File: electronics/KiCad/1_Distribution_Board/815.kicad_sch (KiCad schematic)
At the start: 45 parts, among them J12 Conn_01x06, J13 Conn_01x10, J14 2.54-1*4P母, J15 2.54-1*4P母, J16 PM254V-11-06-H85, J17 Conn_02x08_Odd_Even, J18 PM254V-11-06-H85, J19 2.54-1*4P母, J20 2.54-1*4P母, U6 PCA9306, U7 PCA9685PW, Y1 25MHz

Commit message: Correcting Part rotation for JLCPCB
Several parts needed the "FT Rotation Offset" parameter added to correct for part orientation for JLCPCB order.
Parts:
- U6: LCSC C33196 -> C123752
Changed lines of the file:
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@@
 			)
 		)
-		(property "LCSC" "C33196"
+		(property "LCSC" "C123752"
 			(at 52.07 46.99 0)
 			(effects

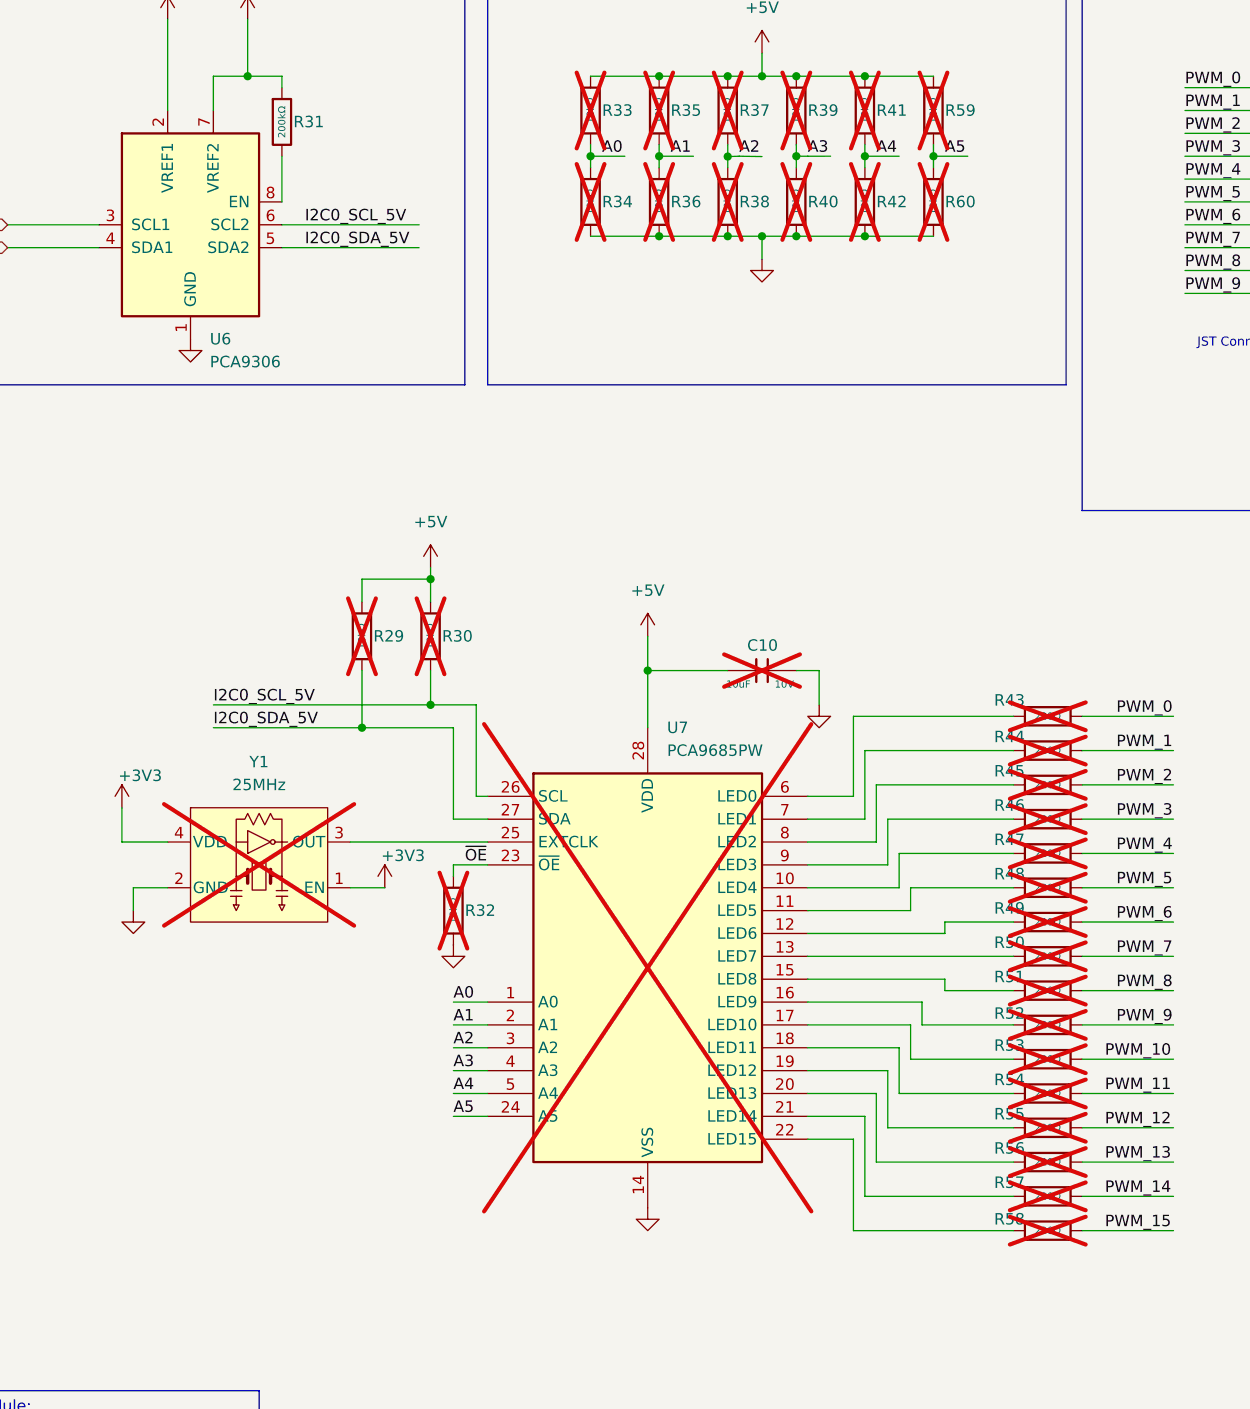
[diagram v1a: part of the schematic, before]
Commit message: Updated to reflect V1.0 of layer board as well
Updated for initial orders with PCA module populated. Also updated to layer boards for flex cables.
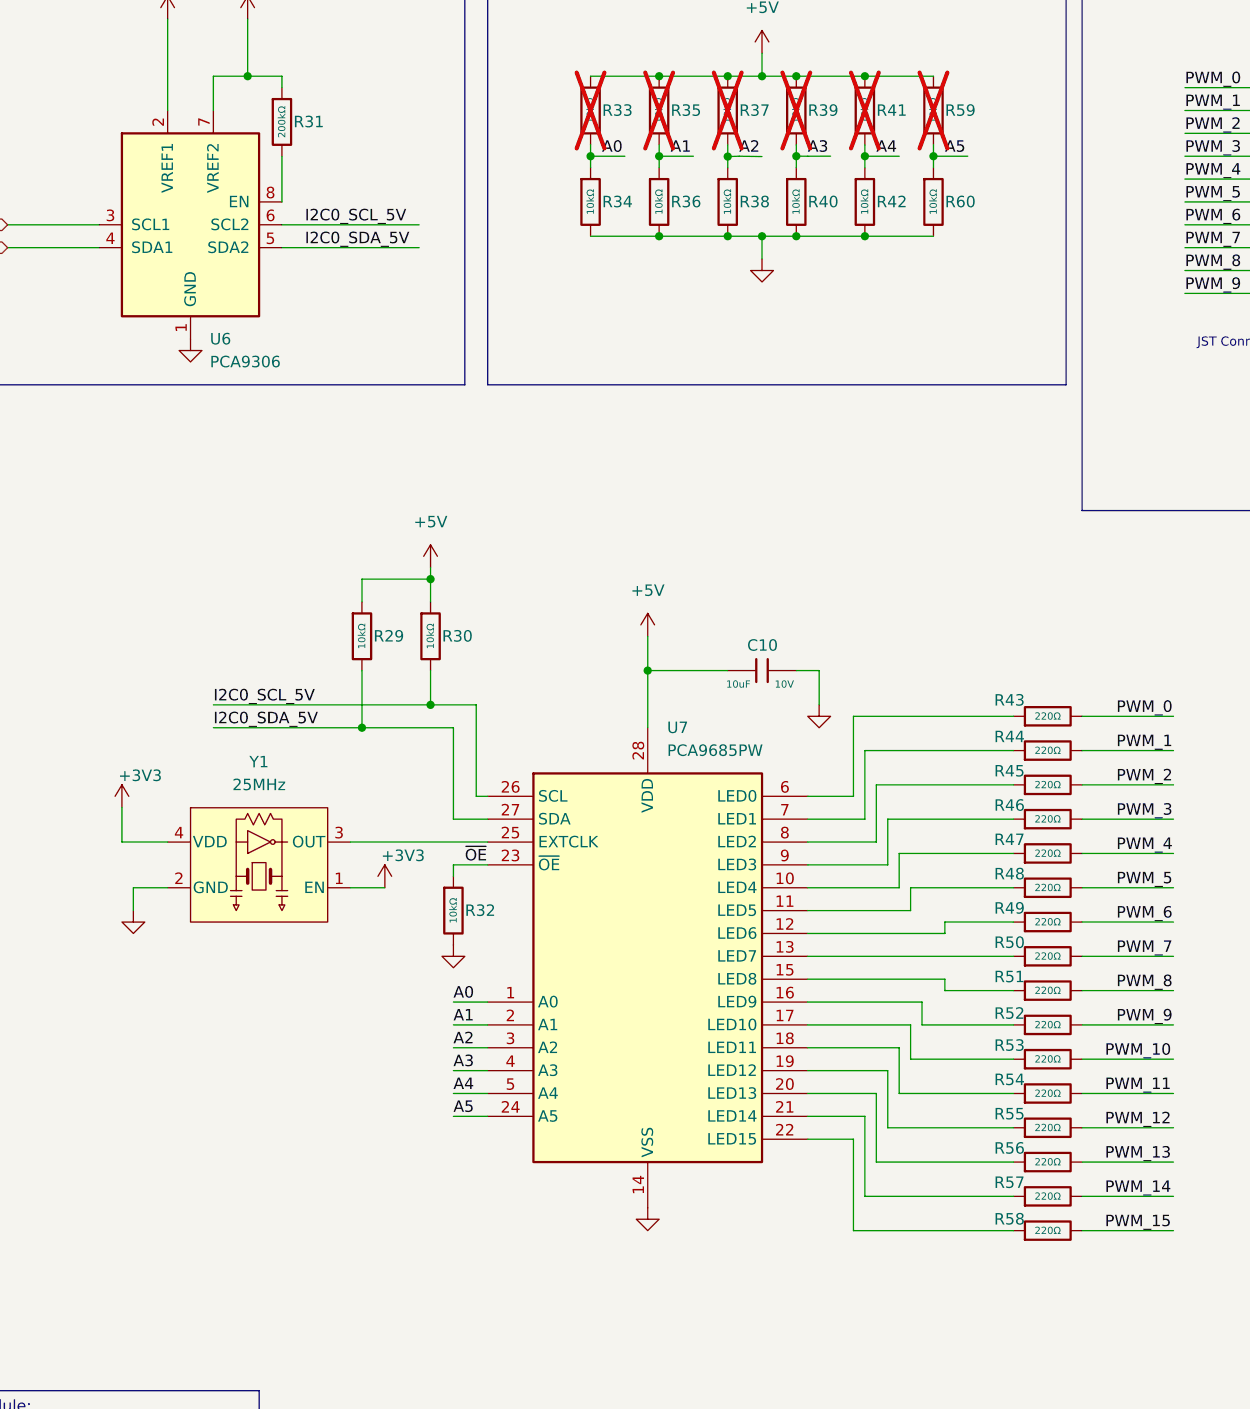
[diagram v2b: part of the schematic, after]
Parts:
- C10, R29, R30, R32, R34, R36, R38, R40, R42, R43, R44, R45, R46, R47, R48, R49, R50, R51, R52, R53, R54, R55, R56, R57, R58, R60, U7, Y1: now fitted
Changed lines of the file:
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@@
 		(in_bom yes)
 		(on_board yes)
-		(dnp yes)
+		(dnp no)
 		(property "Reference" "R53"
 			(at 144.78 138.176 90)
@@
 		(in_bom yes)
 		(on_board yes)
-		(dnp yes)
+		(dnp no)
 		(fields_autoplaced yes)
 		(property "Reference" "U7"
@@
 		(in_bom yes)
 		(on_board yes)
-		(dnp yes)
+		(dnp no)
 		(property "Reference" "R55"
 			(at 144.78 145.796 90)
@@
 		(in_bom yes)
 		(on_board yes)
-		(dnp yes)
+		(dnp no)
 		(property "Reference" "R38"
 			(at 113.03 44.45 0)
@@
 		(in_bom yes)
 		(on_board yes)
-		(dnp yes)
+		(dnp no)
 		(property "Reference" "R50"
 			(at 144.78 126.746 90)
@@
 		(in_bom yes)
 		(on_board yes)
-		(dnp yes)
+		(dnp no)
 		(property "Reference" "R54"
 			(at 144.78 141.986 90)
@@
 		(in_bom yes)
 		(on_board yes)
-		(dnp yes)
+		(dnp no)
 		(property "Reference" "R40"
 			(at 120.65 44.45 0)
@@
 		(in_bom yes)
 		(on_board yes)
-		(dnp yes)
+		(dnp no)
 		(property "Reference" "R52"
 			(at 144.78 134.62 90)
@@
 		(in_bom yes)
 		(on_board yes)
-		(dnp yes)
+		(dnp no)
 		(property "Reference" "R60"
 			(at 135.89 44.45 0)
@@
 		(in_bom yes)
 		(on_board yes)
-		(dnp yes)
+		(dnp no)
 		(property "Reference" "R36"
 			(at 105.41 44.45 0)
@@
 		(in_bom yes)
 		(on_board yes)
-		(dnp yes)
+		(dnp no)
 		(property "Reference" "R34"
 			(at 97.79 44.45 0)
@@
 		(in_bom yes)
 		(on_board yes)
-		(dnp yes)
+		(dnp no)
 		(property "Reference" "R46"
 			(at 144.78 111.506 90)
@@
 		(in_bom yes)
 		(on_board yes)
-		(dnp yes)
+		(dnp no)
 		(property "Reference" "R49"
 			(at 144.78 122.936 90)
@@
 		(in_bom yes)
 		(on_board yes)
-		(dnp yes)
+		(dnp no)
 		(property "Reference" "R42"
 			(at 128.27 44.45 0)
@@
 		(in_bom yes)
 		(on_board yes)
-		(dnp yes)
+		(dnp no)
 		(property "Reference" "R29"
 			(at 72.39 92.71 0)
@@
 		(in_bom yes)
 		(on_board yes)
-		(dnp yes)
+		(dnp no)
 		(fields_autoplaced yes)
 		(property "Reference" "Y1"
@@
 		(in_bom yes)
 		(on_board yes)
-		(dnp yes)
+		(dnp no)
 		(property "Reference" "R44"
 			(at 144.78 103.886 90)
@@
 		(in_bom yes)
 		(on_board yes)
-		(dnp yes)
+		(dnp no)
 		(property "Reference" "R58"
 			(at 144.78 157.48 90)
@@
 		(in_bom yes)
 		(on_board yes)
-		(dnp yes)
+		(dnp no)
 		(property "Reference" "R45"
 			(at 144.78 107.696 90)
@@
 		(in_bom yes)
 		(on_board yes)
-		(dnp yes)
+		(dnp no)
 		(property "Reference" "R43"
 			(at 144.78 99.822 90)
@@
 		(in_bom yes)
 		(on_board yes)
-		(dnp yes)
+		(dnp no)
 		(property "Reference" "R47"
 			(at 144.78 115.316 90)
@@
 		(in_bom yes)
 		(on_board yes)
-		(dnp yes)
+		(dnp no)
 		(property "Reference" "R48"
 			(at 144.78 119.126 90)
@@
 		(in_bom yes)
 		(on_board yes)
-		(dnp yes)
+		(dnp no)
 		(property "Reference" "R56"
 			(at 144.78 149.606 90)
@@
 		(in_bom yes)
 		(on_board yes)
-		(dnp yes)
+		(dnp no)
 		(property "Reference" "R30"
 			(at 80.01 92.71 0)
@@
 		(in_bom yes)
 		(on_board yes)
-		(dnp yes)
+		(dnp no)
 		(property "Reference" "R51"
 			(at 144.78 130.556 90)
@@
 		(in_bom yes)
 		(on_board yes)
-		(dnp yes)
+		(dnp no)
 		(property "Reference" "C10"
 			(at 117.348 93.726 90)
@@
 		(in_bom yes)
 		(on_board yes)
-		(dnp yes)
+		(dnp no)
 		(property "Reference" "R57"
 			(at 144.78 153.416 90)
@@
 		(in_bom yes)
 		(on_board yes)
-		(dnp yes)
+		(dnp no)
 		(property "Reference" "R32"
 			(at 82.55 123.19 0)

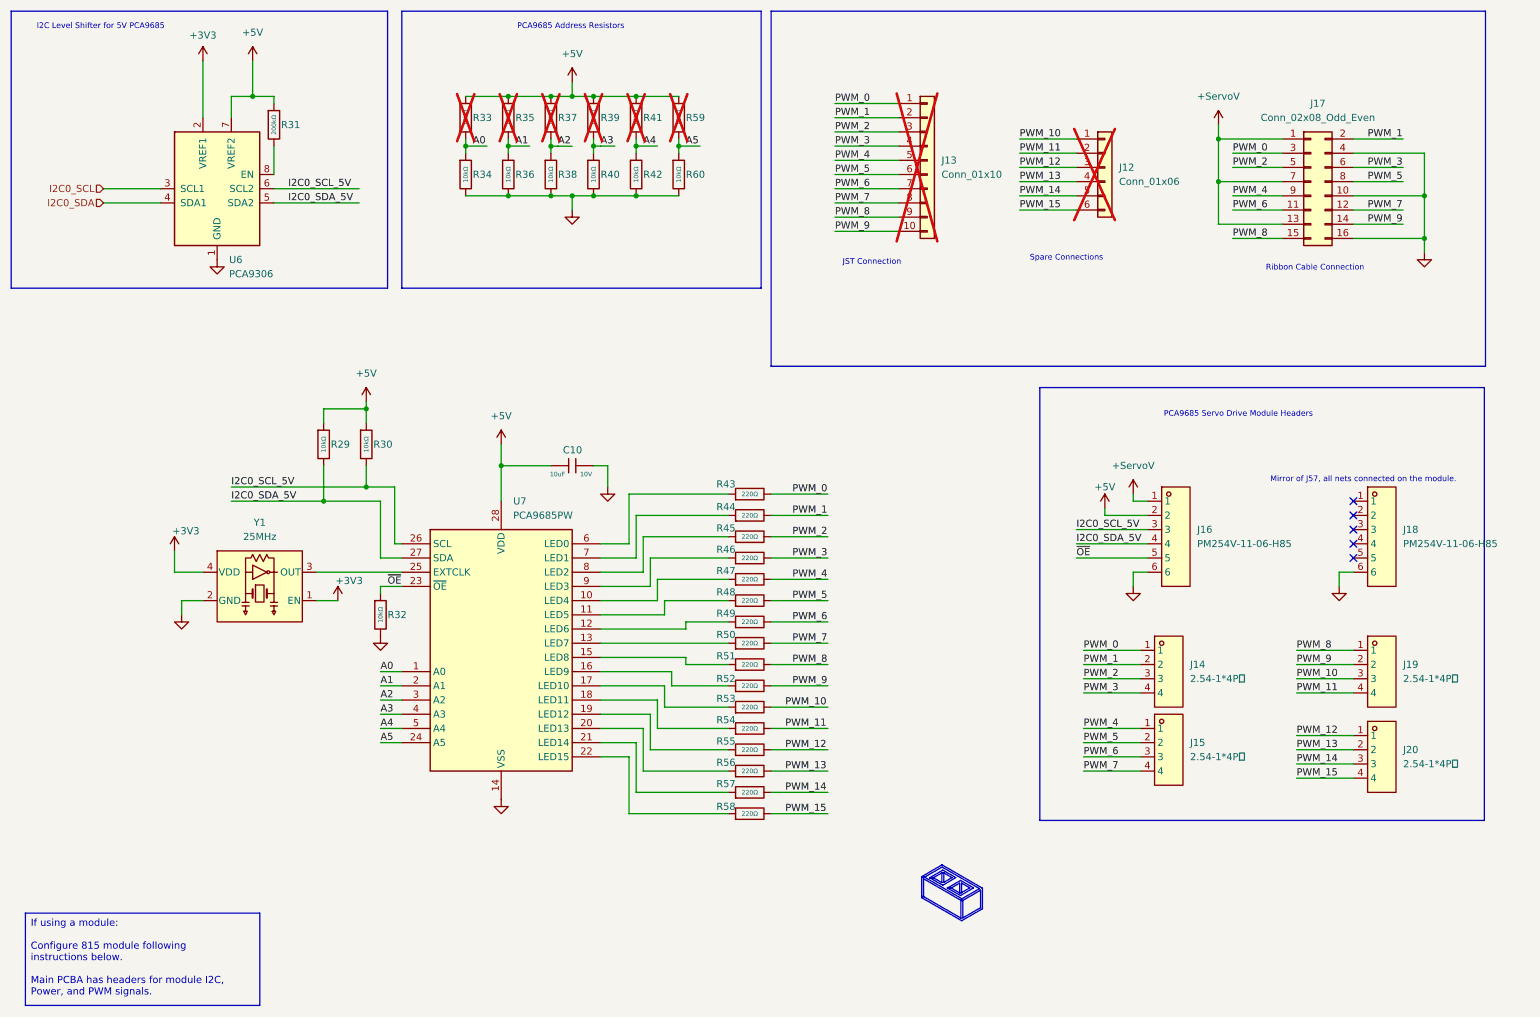
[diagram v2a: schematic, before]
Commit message: Corrected SCH for power sequence issue
5V to Vsys for all powered items.
Correction of the PCA9306 power pins.
Added decoupling to oscillator and PCA9306.
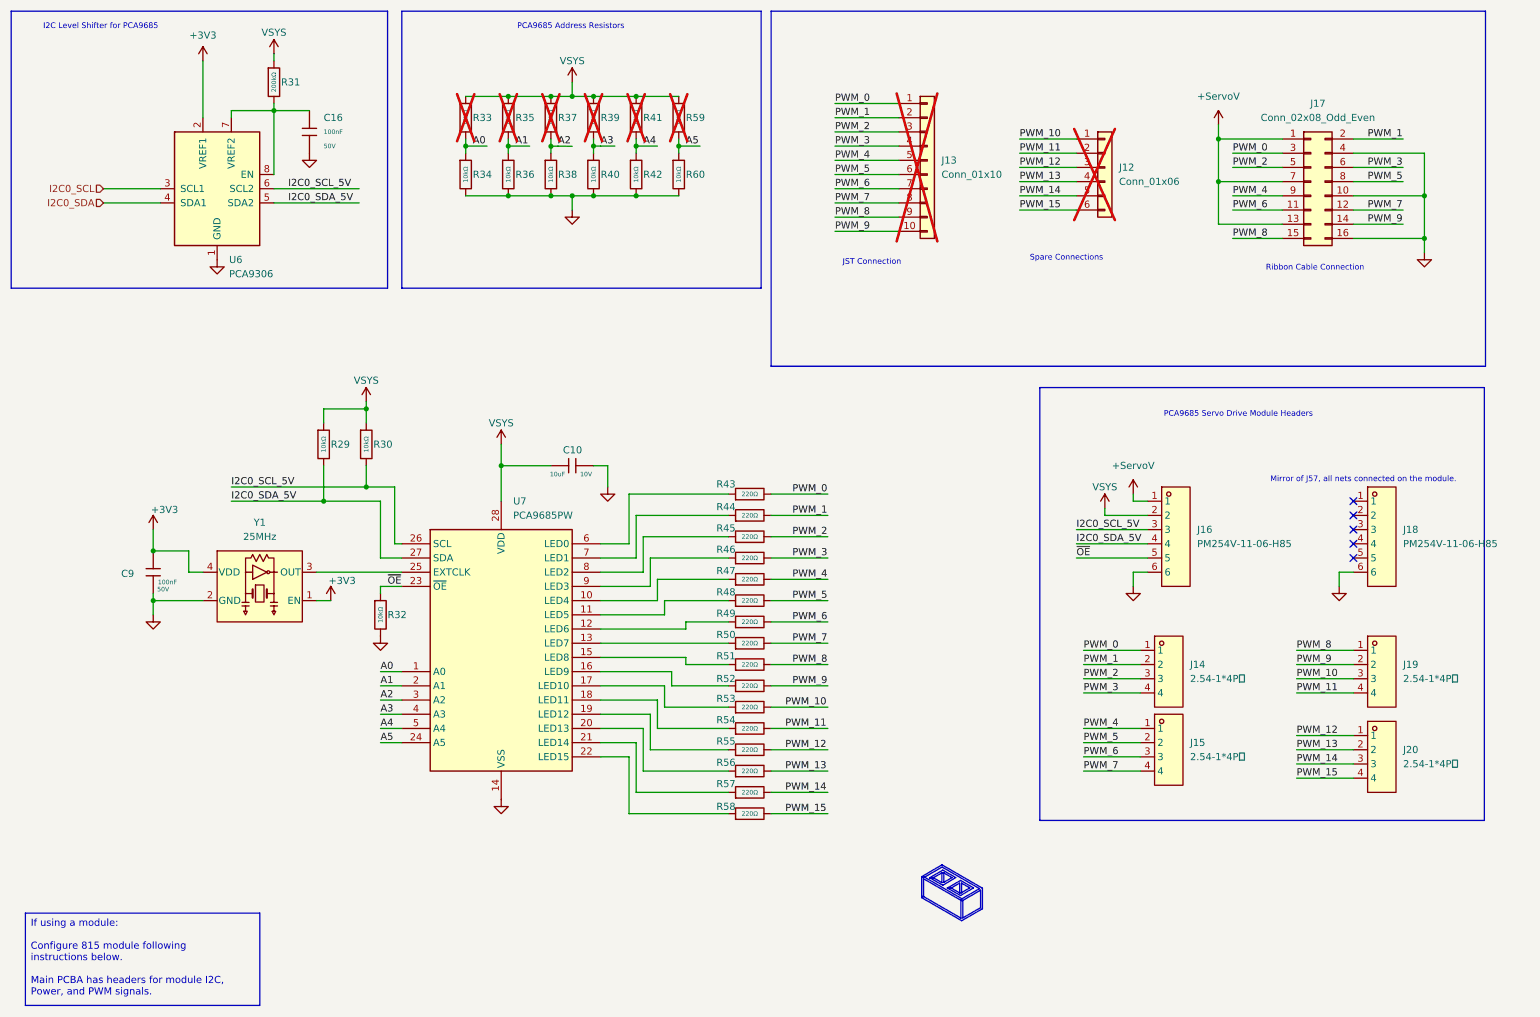
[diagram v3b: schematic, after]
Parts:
- added C16, C9: 100nF, PCM_JLCPCB:C_0603, symbol PCM_JLCPCB-Capacitors:0603,100nF
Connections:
- net +3V3: now also C9.2
- net GND: now also C16.2, C9.1
- net at R31.2, U6.8 (EN): now also U6.7 (VREF2), C16.1
- net +5V renamed VSYS
- net VSYS: no longer U6.7 (VREF2)
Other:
- note added: "I2C Level Shifter for PCA9685"
- note removed: "I2C Level Shifter for 5V PCA9685"
- moved on the sheet: R31
